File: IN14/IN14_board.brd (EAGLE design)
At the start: 35 x 50 mm, 28 parts, among them T1 BC848, T10 BC848, T11 BC848, T12 BC848, T2 BC848, T3 BC848, T4 BC848, T5 BC848, T6 BC848, T7 BC848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

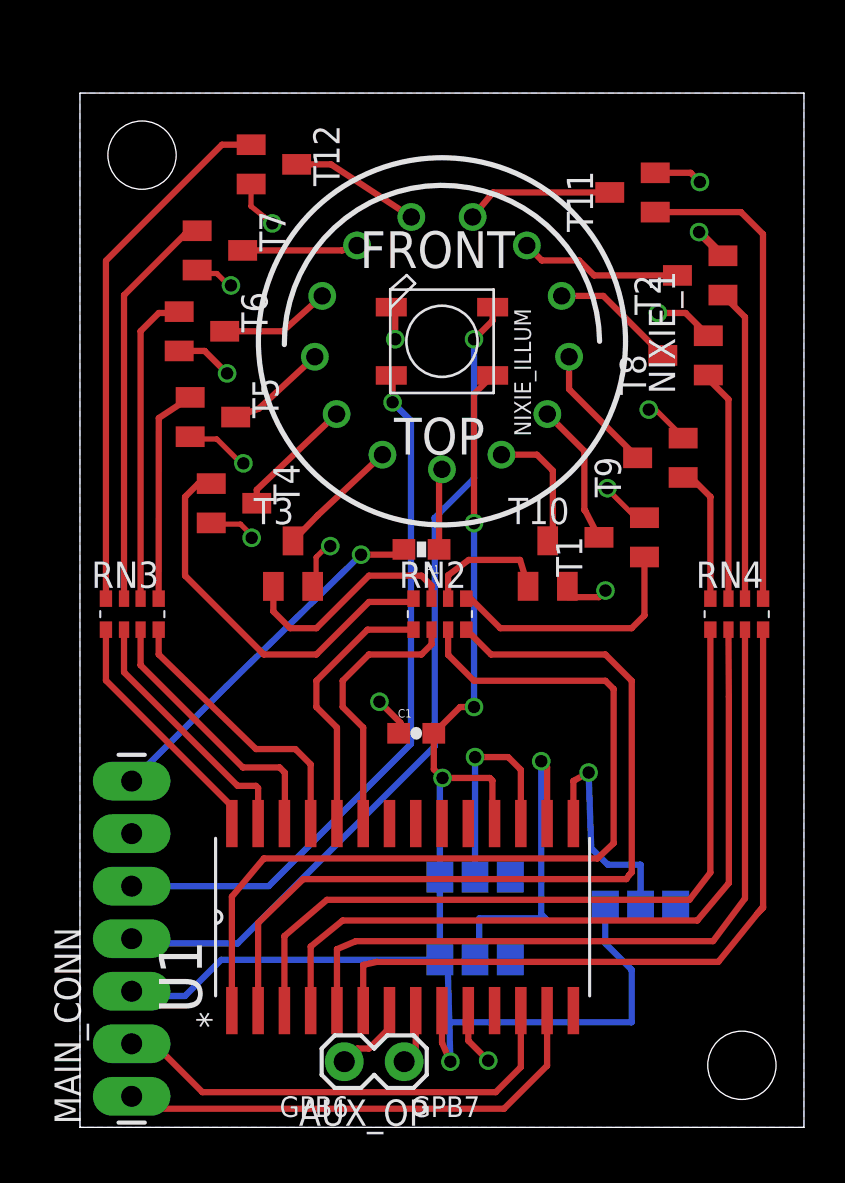
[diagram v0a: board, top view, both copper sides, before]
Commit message: Added files via upload
New 'thinner' board - now revision 1.2.  Pincompatible with previous bus-driven designs, but library code will need to be adjusted as the pins are mapped differently for economy of space!
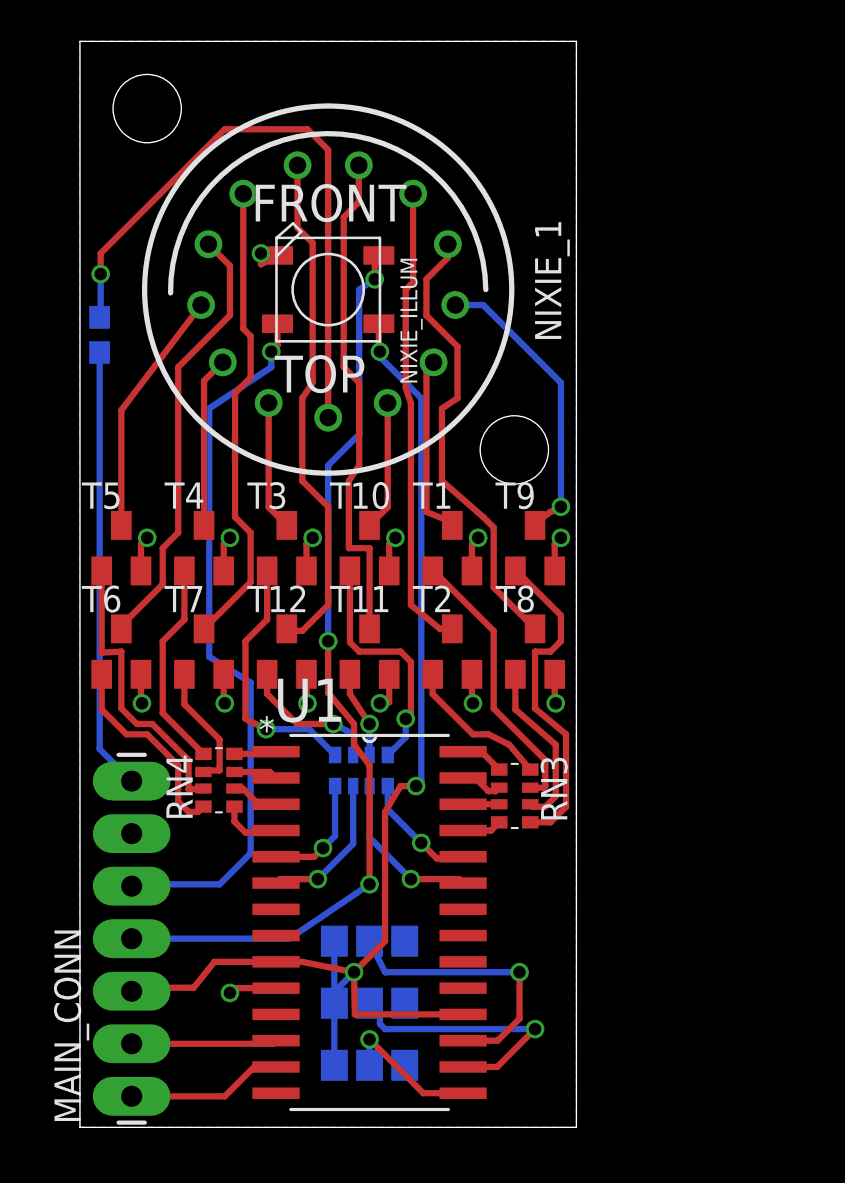
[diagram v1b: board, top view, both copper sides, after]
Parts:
- removed AUX_OP: (no value), SparkFun-Connectors:1X02_LOCK
- removed C1: 0.1uF, SparkFun-Capacitors:0603-CAP
- removed U$4: (no value), SparkFun-Electromechanical:STAND-OFF
- added U$5: (no value), SparkFun-Electromechanical:STAND-OFF
- moved RN4 26.3 mm to (6.72, 16.8), turned to 90 degrees
- moved T11 25.6 mm to (14.0, 23.0), turned to 0 degrees
- moved T12 23.6 mm to (10.0, 23.0), turned to 0 degrees
- moved T2 21.8 mm to (18.0, 23.0), turned to 0 degrees
- moved RN3 20.5 mm to (21.0, 16.0), turned to 270 degrees
- moved T7 19.4 mm to (6.00, 23.0), turned to 0 degrees
- moved R1 18.7 mm to (0.95, 38.3), flipped to the bottom, turned to 270 degrees
- moved T8 16.1 mm to (22.0, 23.0), turned to 0 degrees
- moved T6 16.0 mm to (2.00, 23.0), turned to 0 degrees
- moved JMP1 15.2 mm to (14.0, 3.00)
- moved T10 8.64 mm to (14.0, 28.0)
- moved RN2 8.46 mm to (13.6, 17.2), flipped to the bottom
- moved T1 8.21 mm to (18.0, 28.0), turned to 0 degrees
- moved T5 7.73 mm to (2.00, 28.0), turned to 0 degrees
- moved T9 7.47 mm to (22.0, 28.0), turned to 0 degrees
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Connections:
- removed net N$21: RN2.6, T10.1
- new net N$16: RN2.8, T10.1
- net CTL_CAT0: now also RN4.3; no longer RN2.4
- net CTL_CAT6: now also RN2.3; no longer RN4.4
- net CTL_CAT7: now also RN2.4; no longer RN4.3
- net CTL_CAT8: now also RN4.1; no longer RN4.2
- net CTL_CAT9: now also RN4.2; no longer RN4.1
- net CTL_CAT_LHDP: now also RN4.4; no longer RN2.3
- net GND: no longer C1.1
- net N$1: now also T2.1; no longer T12.1
- net N$10: now also RN4.8, T6.1; no longer RN4.5, T11.1
- net N$11: now also T9.1; no longer T5.1
- net N$12: now also T5.1; no longer T8.1
- net N$13: now also RN4.6, T7.1; no longer RN3.6, T6.1
- net N$14: now also RN2.6, T12.1; no longer RN4.8, T9.1
- net N$15: now also RN2.7, T11.1; no longer RN3.7, T7.1
- net N$3: now also RN3.7; no longer RN2.5
- net N$5: now also RN3.6, T8.1; no longer RN4.6, T2.1
- net N$7: now also RN2.5; no longer RN2.7
- net N$9: now also RN4.5; no longer RN2.8
- net NC3: no longer AUX_OP.2
- net NC4: no longer AUX_OP.1
- net VCC: no longer C1.2
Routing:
- net CTL_CAT_LHDP: track 42.5 -> 2.05 mm
- net CTL_CAT0: track 41.6 -> 2.13 mm
- net CTL_CAT9: track 37.2 -> 2.42 mm
- net CTL_CAT8: track 36.9 -> 2.99 mm
- net CTL_CAT7: track 36.8 -> 5.69 mm, vias 0 -> 1
- net CTL_CAT6: track 36.6 -> 7.31 mm, vias 0 -> 1
- net N$4: track 3.93 -> 30.0 mm, vias 0 -> 1
- net CAT_5: track 6.30 -> 24.8 mm
- net N$1: track 25.7 -> 7.15 mm
- net CAT_4: track 5.57 -> 22.7 mm
- net CAT_6: track 7.19 -> 24.2 mm
- net SDA: track 23.8 -> 7.63 mm
- net CAT_8: track 6.08 -> 22.0 mm
- net SCL: track 22.9 -> 7.04 mm
- net CAT_3: track 5.37 -> 21.2 mm
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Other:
- board size 35 x 50 mm -> 24 x 52.5 mm
- board text added: "Nixie I2C IN14 v1.2"
- board text removed: "GPB6"
- board text removed: "GPB7"
- board text removed: "Nixie I2C IN14 v1.1"

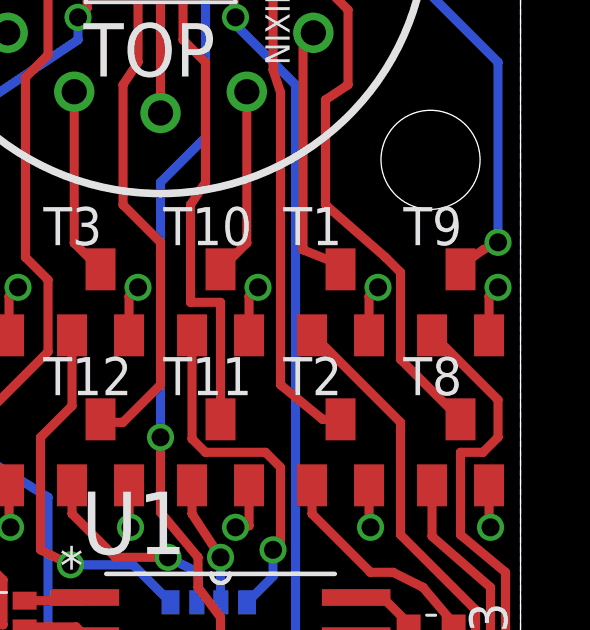
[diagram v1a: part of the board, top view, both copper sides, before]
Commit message: Moved files in together!
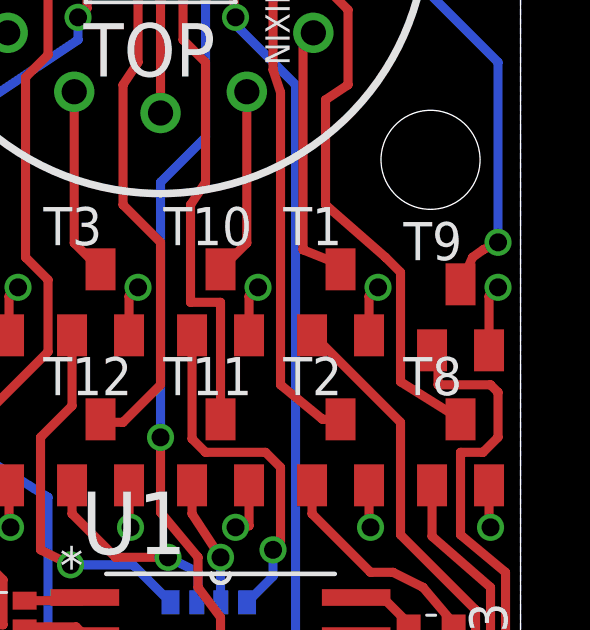
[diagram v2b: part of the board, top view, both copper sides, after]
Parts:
- moved T9 0.50 mm to (22.0, 27.5)
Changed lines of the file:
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@@
 <layer number="21" name="tPlace" color="16" fill="1" visible="yes" active="yes"/>
 <layer number="22" name="bPlace" color="14" fill="1" visible="yes" active="yes"/>
-<layer number="23" name="tOrigins" color="15" fill="1" visible="no" active="yes"/>
+<layer number="23" name="tOrigins" color="15" fill="1" visible="yes" active="yes"/>
 <layer number="24" name="bOrigins" color="15" fill="1" visible="no" active="yes"/>
 <layer number="25" name="tNames" color="7" fill="1" visible="no" active="yes"/>
@@
 <layer number="37" name="tTest" color="7" fill="1" visible="no" active="yes"/>
 <layer number="38" name="bTest" color="7" fill="1" visible="no" active="yes"/>
-<layer number="39" name="tKeepout" color="4" fill="11" visible="no" active="yes"/>
-<layer number="40" name="bKeepout" color="1" fill="11" visible="no" active="yes"/>
+<layer number="39" name="tKeepout" color="4" fill="11" visible="yes" active="yes"/>
+<layer number="40" name="bKeepout" color="1" fill="11" visible="yes" active="yes"/>
 <layer number="41" name="tRestrict" color="4" fill="10" visible="no" active="yes"/>
 <layer number="42" name="bRestrict" color="1" fill="10" visible="no" active="yes"/>
@@
 <element name="T7" library="transistor" package="SOT23" value="BC848" x="6" y="23"/>
 <element name="T8" library="transistor" package="SOT23" value="BC848" x="22" y="23"/>
-<element name="T9" library="transistor" package="SOT23" value="BC848" x="22" y="28"/>
+<element name="T9" library="transistor" package="SOT23" value="BC848" x="22" y="27.5"/>
 <element name="T10" library="transistor" package="SOT23" value="BC848" x="14" y="28"/>
 <element name="T11" library="transistor" package="SOT23" value="BC848" x="14" y="23"/>
@@
 <wire x1="18.95" y1="26.9" x2="18.95" y2="28.2" width="0.3048" layer="1"/>
 <wire x1="18.95" y1="28.2" x2="19.25" y2="28.5" width="0.3048" layer="1"/>
-<wire x1="22.95" y1="26.9" x2="22.95" y2="28.2" width="0.3048" layer="1"/>
+<wire x1="22.95" y1="26.4" x2="22.95" y2="28.2" width="0.3048" layer="1"/>
 <wire x1="22.95" y1="28.2" x2="23.25" y2="28.5" width="0.3048" layer="1"/>
 <via x="3" y="20.5" extent="1-16" drill="0.6"/>
@@
 <wire x1="17.5" y1="31.25" x2="19.5" y2="29.5" width="0.3048" layer="1"/>
 <wire x1="19.5" y1="29.5" x2="20" y2="29" width="0.3048" layer="1"/>
-<wire x1="20" y1="29" x2="20" y2="26.1" width="0.3048" layer="1"/>
-<wire x1="20" y1="26.1" x2="22" y2="24.1" width="0.3048" layer="1"/>
+<wire x1="20" y1="29" x2="20" y2="25.35" width="0.3048" layer="1"/>
+<wire x1="20" y1="25.35" x2="22" y2="24.1" width="0.3048" layer="1"/>
 </signal>
 <signal name="CAT_9">
@@
 <wire x1="23.25" y1="30" x2="22.75" y2="29.75" width="0.3048" layer="1"/>
 <wire x1="22.75" y1="29.75" x2="22.4" y2="29.5" width="0.3048" layer="1"/>
-<wire x1="22.4" y1="29.5" x2="22" y2="29.1" width="0.3048" layer="1"/>
+<wire x1="22.4" y1="29.5" x2="22" y2="28.6" width="0.3048" layer="1"/>
 </signal>
 <signal name="CAT_0">
@@
 <contactref element="T9" pad="1"/>
 <contactref element="RN3" pad="5"/>
-<wire x1="21.05" y1="26.9" x2="21.1" y2="26.9" width="0.3048" layer="1"/>
-<wire x1="21.1" y1="26.9" x2="23.25" y2="24.75" width="0.3048" layer="1"/>
-<wire x1="23.25" y1="24.75" x2="23.25" y2="23.5" width="0.3048" layer="1"/>
 <wire x1="23.25" y1="23.5" x2="22.75" y2="23" width="0.3048" layer="1"/>
 <wire x1="22.75" y1="23" x2="22" y2="23" width="0.3048" layer="1"/>
@@
 <wire x1="23.5" y1="15.5" x2="22.745" y2="14.745" width="0.3048" layer="1"/>
 <wire x1="21.77" y1="14.745" x2="22.745" y2="14.745" width="0.3048" layer="1"/>
+<wire x1="23.25" y1="23.5" x2="23.25" y2="25" width="0.3048" layer="1"/>
+<wire x1="23.25" y1="25" x2="23" y2="25.25" width="0.3048" layer="1"/>
+<wire x1="23" y1="25.25" x2="21.25" y2="25.25" width="0.3048" layer="1"/>
+<wire x1="21.25" y1="25.25" x2="21.25" y2="26.2" width="0.3048" layer="1"/>
+<wire x1="21.25" y1="26.2" x2="21.05" y2="26.4" width="0.3048" layer="1"/>
 </signal>
 <signal name="N$10">
